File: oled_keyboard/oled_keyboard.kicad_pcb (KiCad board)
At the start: 4 copper layers, 100 x 100 mm, 126 parts, among them J1 Conn_01x20_Socket, J10 Conn_01x20_Socket, J11 Conn_01x20_Socket, J12 Conn_01x20_Socket, J2 Conn_01x20_Socket, J3 Conn_01x20_Socket, J4 Conn_01x20_Socket, J5 Conn_01x20_Socket, J6 Conn_01x20_Socket, J7 Conn_01x20_Socket, J8 Conn_01x20_Socket, J9 Conn_01x20_Socket, SW1 SW_Push, SW10 SW_Push, SW11 SW_Push, SW12 SW_Push, SW2 SW_Push, SW3 SW_Push, SW4 SW_Push, SW5 SW_Push, SW6 SW_Push, SW7 SW_Push, SW8 SW_Push, SW9 SW_Push, U1 TPS61088RHLR

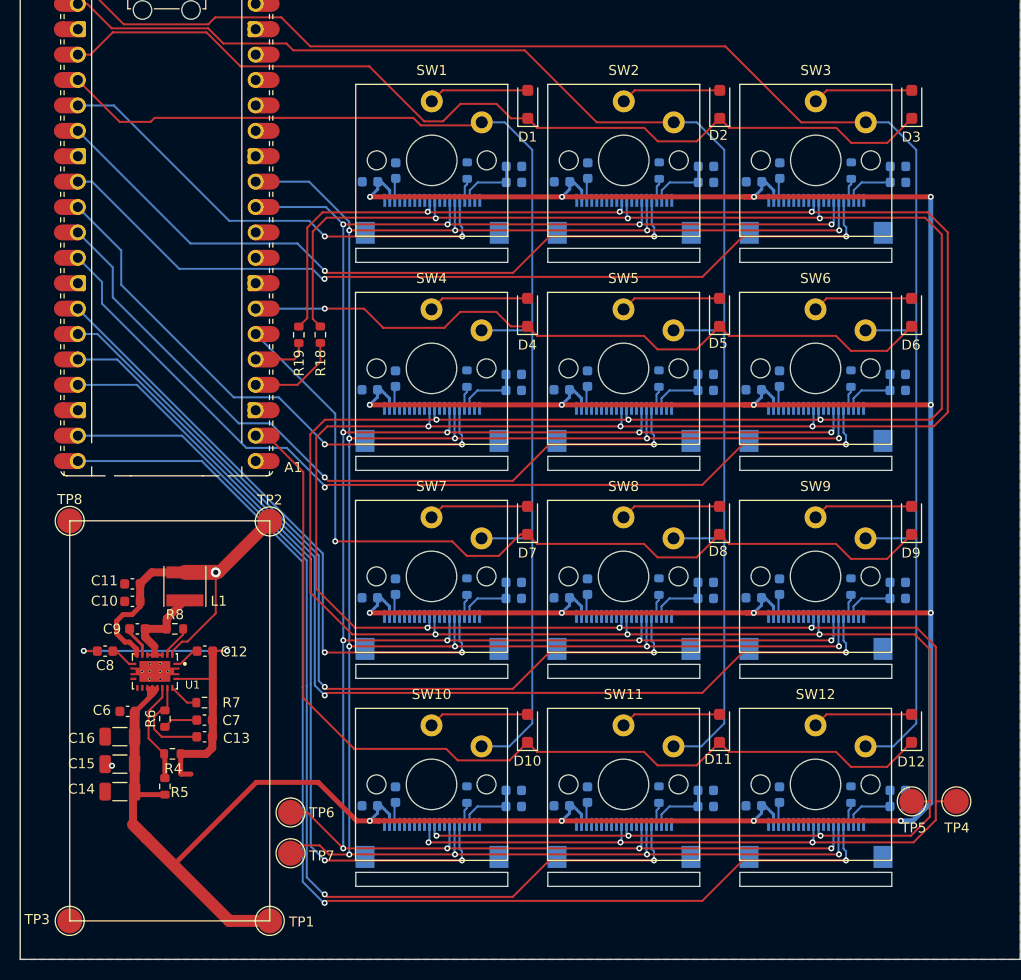
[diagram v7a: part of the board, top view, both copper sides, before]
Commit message: fix: added 3v3! enlarged holes for passing naps
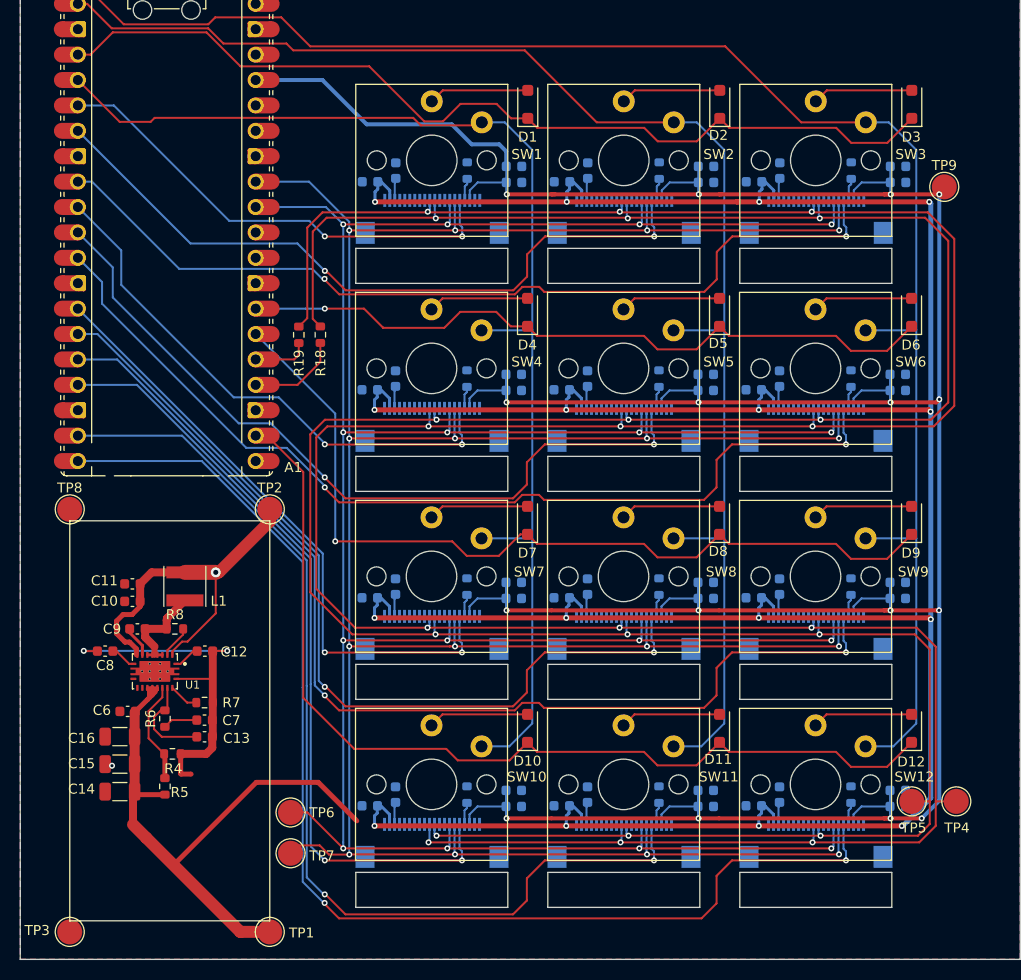
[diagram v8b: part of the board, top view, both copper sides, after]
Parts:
- added TP9: TestPoint, TestPoint:TestPoint_Pad_D2.5mm, F.Cu at (174.2, 53.2)
- moved TP2 1.20 mm to (106.8, 85.5)
- moved TP8 1.15 mm to (86.8, 85.5)
- moved TP1 1.10 mm to (106.8, 127.8)
- moved TP3 1.10 mm to (86.8, 127.8)
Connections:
- A1 pad 36: unconnected-(A1-3V3-Pad36) -> 3V3
- C18 pad 1: Net-(J2-Pin_3) -> 3V3
- C19 pad 1: Net-(J2-Pin_3) -> 3V3
- C2 pad 1: Net-(J1-Pin_3) -> 3V3
- C21 pad 1: Net-(J4-Pin_3) -> 3V3
- C23 pad 1: Net-(J4-Pin_3) -> 3V3
- C24 pad 1: Net-(J3-Pin_3) -> 3V3
- C26 pad 1: Net-(J3-Pin_3) -> 3V3
- C31 pad 1: Net-(J8-Pin_3) -> 3V3
- C35 pad 1: Net-(J8-Pin_3) -> 3V3
- C36 pad 1: Net-(J5-Pin_3) -> 3V3
- C37 pad 1: Net-(J6-Pin_3) -> 3V3
- C38 pad 1: Net-(J7-Pin_3) -> 3V3
- C4 pad 1: Net-(J1-Pin_3) -> 3V3
- C40 pad 1: Net-(J5-Pin_3) -> 3V3
- C41 pad 1: Net-(J6-Pin_3) -> 3V3
- C42 pad 1: Net-(J7-Pin_3) -> 3V3
- C47 pad 1: Net-(J12-Pin_3) -> 3V3
- C51 pad 1: Net-(J12-Pin_3) -> 3V3
- C52 pad 1: Net-(J9-Pin_3) -> 3V3
- C53 pad 1: Net-(J10-Pin_3) -> 3V3
- C54 pad 1: Net-(J11-Pin_3) -> 3V3
- C56 pad 1: Net-(J9-Pin_3) -> 3V3
- C57 pad 1: Net-(J10-Pin_3) -> 3V3
- C58 pad 1: Net-(J11-Pin_3) -> 3V3
- J1 pad 3: Net-(J1-Pin_3) -> 3V3
- J10 pad 3: Net-(J10-Pin_3) -> 3V3
- J11 pad 3: Net-(J11-Pin_3) -> 3V3
- J12 pad 3: Net-(J12-Pin_3) -> 3V3
- J2 pad 3: Net-(J2-Pin_3) -> 3V3
- J3 pad 3: Net-(J3-Pin_3) -> 3V3
- J4 pad 3: Net-(J4-Pin_3) -> 3V3
- J5 pad 3: Net-(J5-Pin_3) -> 3V3
- J6 pad 3: Net-(J6-Pin_3) -> 3V3
- J7 pad 3: Net-(J7-Pin_3) -> 3V3
- J8 pad 3: Net-(J8-Pin_3) -> 3V3
- J9 pad 3: Net-(J9-Pin_3) -> 3V3
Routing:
- net 3V3: track 0.00 -> 360.2 mm, vias 0 -> 16
- net Net-(J1-Pin_3): track 6.58 -> 0.00 mm
- net Net-(J4-Pin_3): track 6.58 -> 0.00 mm
- net Net-(J3-Pin_3): track 6.58 -> 0.00 mm
- net Net-(J2-Pin_3): track 6.58 -> 0.00 mm
- net Net-(J12-Pin_3): track 6.58 -> 0.00 mm
- net Net-(J11-Pin_3): track 6.58 -> 0.00 mm
- net Net-(J10-Pin_3): track 6.58 -> 0.00 mm
- net Net-(J5-Pin_3): track 6.58 -> 0.00 mm
- net Net-(J8-Pin_3): track 6.58 -> 0.00 mm
- net Net-(J7-Pin_3): track 6.58 -> 0.00 mm
- net Net-(J6-Pin_3): track 6.58 -> 0.00 mm
- net Net-(J9-Pin_3): track 6.58 -> 0.00 mm
- net /CS3: track 86.3 -> 90.0 mm
- net /CS9: track 103.7 -> 107.1 mm
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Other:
- outline, holes or cut-outs redrawn
